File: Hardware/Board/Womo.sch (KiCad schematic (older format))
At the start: 0 parts

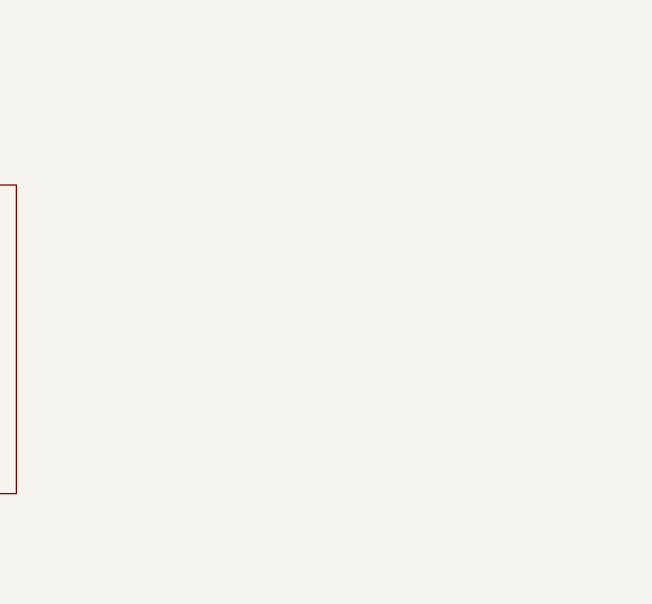
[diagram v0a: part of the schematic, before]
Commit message: FTDI EVE Touch hinzugefügt
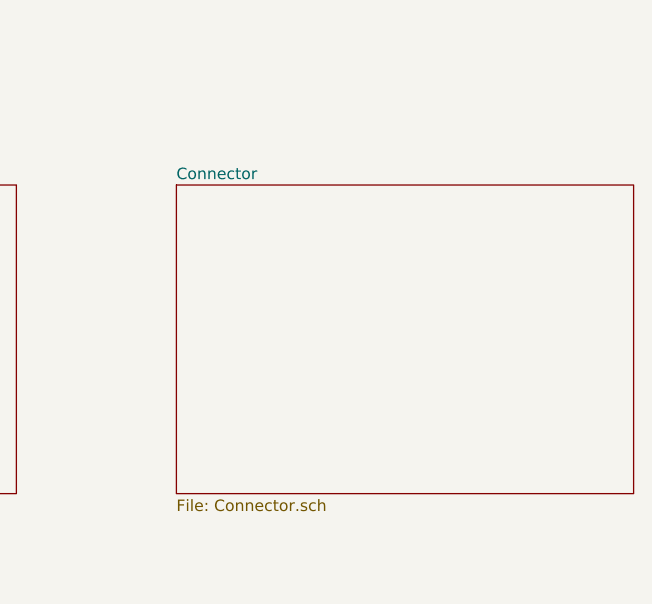
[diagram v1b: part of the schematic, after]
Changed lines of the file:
@@
 $Descr A4 11693 8268
 encoding utf-8
-Sheet 1 6
+Sheet 1 7
 Title ""
 Date ""
@@
 F1 "Sensor.sch" 50
 $EndSheet
+$Sheet
+S 6850 3450 2000 1350
+U 5CC9A992
+F0 "Connector" 50
+F1 "Connector.sch" 50
+$EndSheet
 $EndSCHEMATC

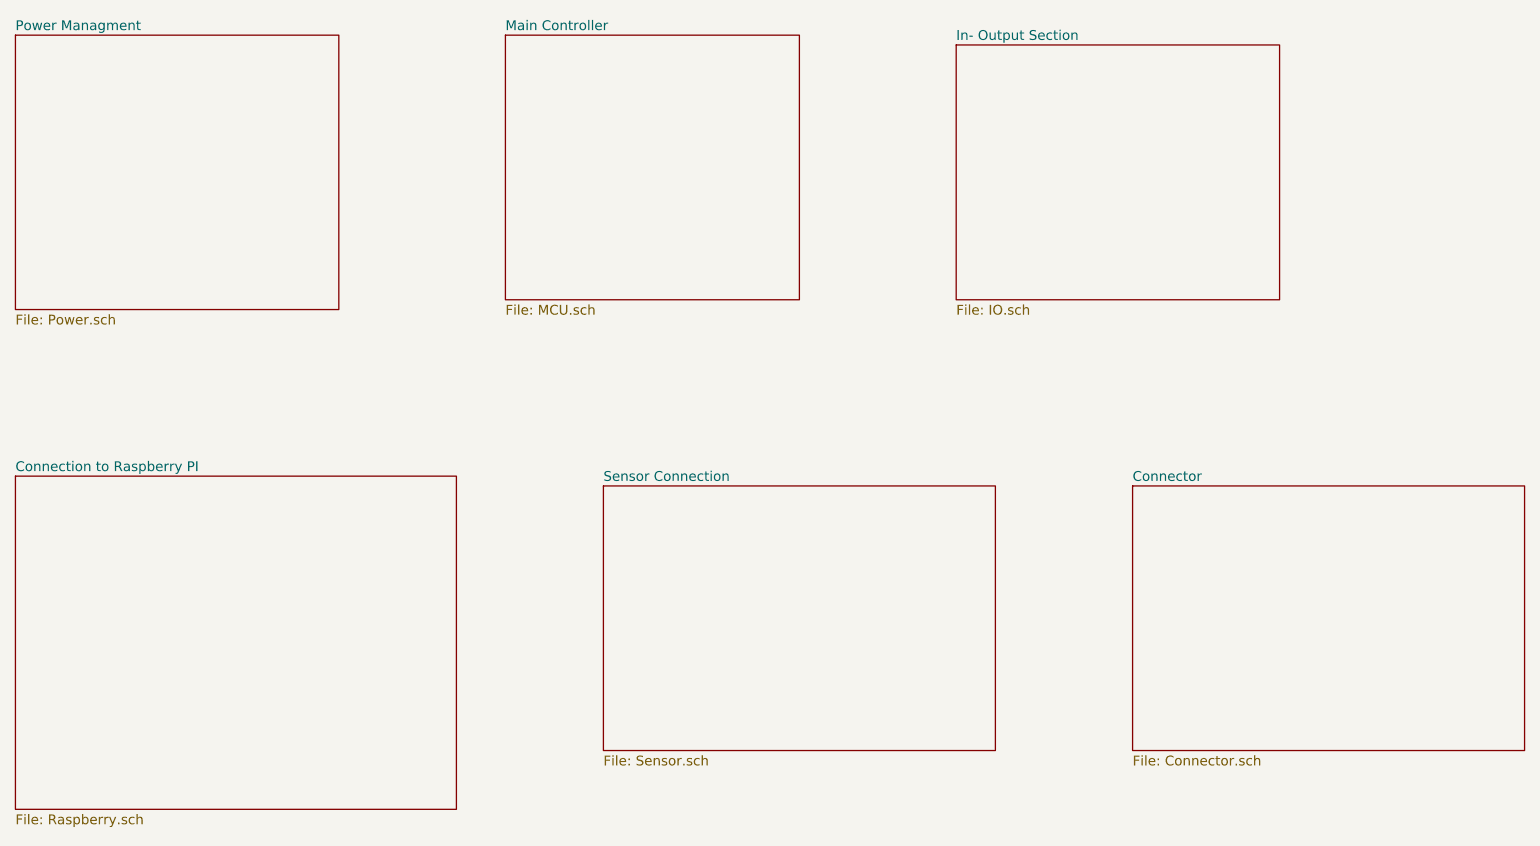
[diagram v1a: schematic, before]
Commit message: Netzliste und Board erstellt, hier sind noch Fehler im Bereich Footprints, BLE Modul nRF8001 hinzugefügt, erste Anschlussklemmen zugefügt
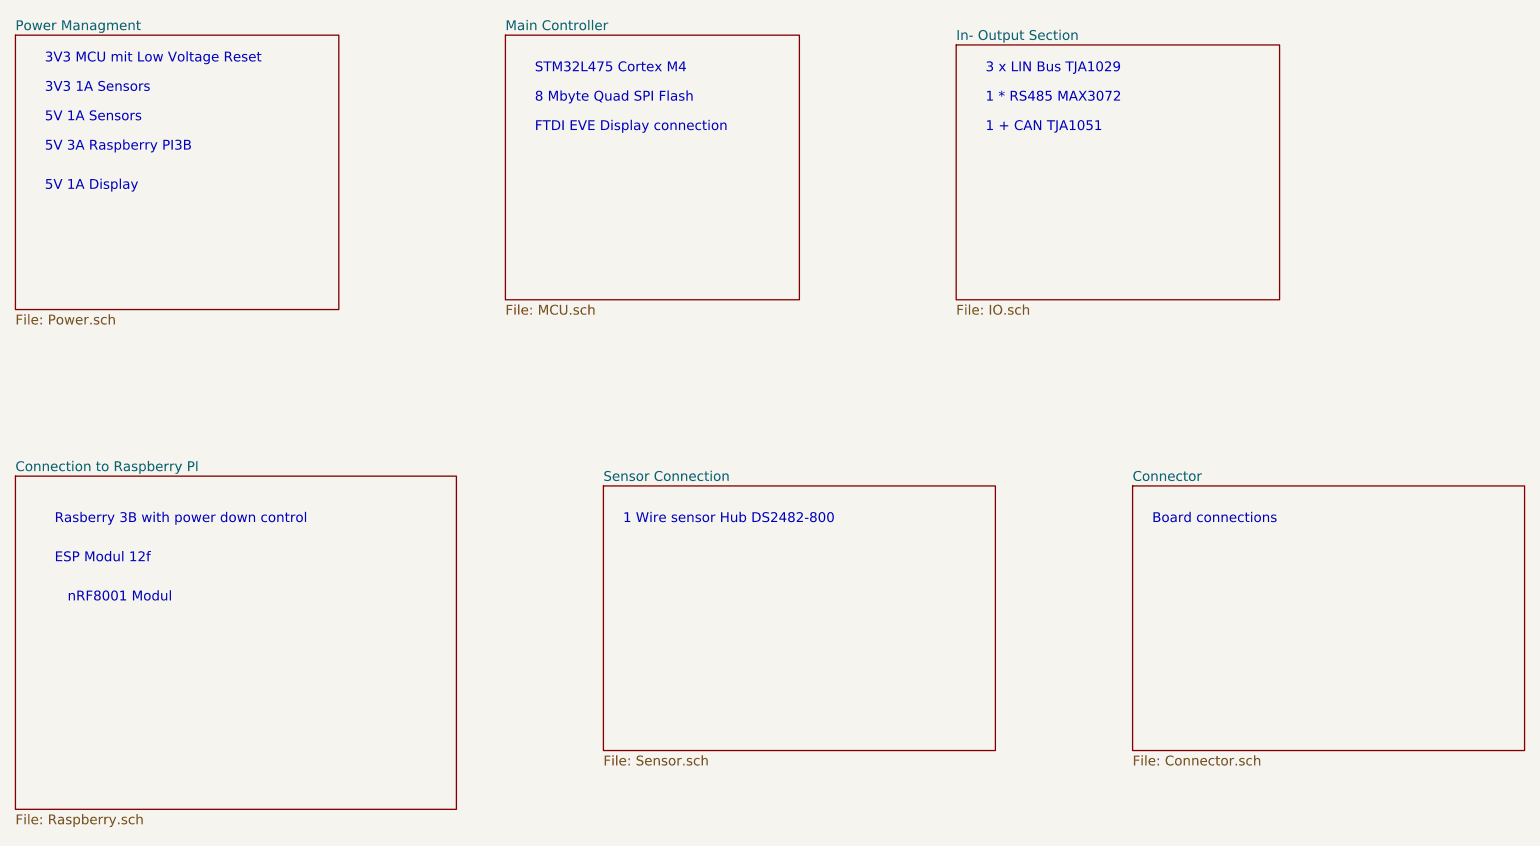
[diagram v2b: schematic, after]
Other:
- note added: "1 * RS485 MAX3072\n"
- note added: "1 + CAN TJA1051\n"
- note added: "1 Wire sensor Hub DS2482-800"
- note added: "3 x LIN Bus TJA1029\n"
- note added: "3V3 1A Sensors"
- note added: "3V3 MCU mit Low Voltage Reset"
- note added: "5V 1A Display"
- note added: "5V 1A Sensors"
- note added: "5V 3A Raspberry PI3B"
- note added: "8 Mbyte Quad SPI Flash\n"
- note added: "Board connections"
- note added: "ESP Modul 12f"
- note added: "FTDI EVE Display connection\n"
- note added: "Rasberry 3B with power down control"
- note added: "STM32L475 Cortex M4\n"
- note added: "nRF8001 Modul\n"
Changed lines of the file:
@@
 F1 "Connector.sch" 50
 $EndSheet
+Text Notes 1300 1300 0    50   ~ 0
+3V3 MCU mit Low Voltage Reset
+Text Notes 1300 1450 0    50   ~ 0
+3V3 1A Sensors
+Text Notes 1300 1600 0    50   ~ 0
+5V 1A Sensors
+Text Notes 1300 1750 0    50   ~ 0
+5V 3A Raspberry PI3B
+Text Notes 1300 1950 0    50   ~ 0
+5V 1A Display
+Text Notes 3800 1350 0    50   ~ 0
+STM32L475 Cortex M4\n
+Text Notes 3800 1500 0    50   ~ 0
+8 Mbyte Quad SPI Flash\n
+Text Notes 3800 1650 0    50   ~ 0
+FTDI EVE Display connection\n
+Text Notes 6100 1350 0    50   ~ 0
+3 x LIN Bus TJA1029\n
+Text Notes 6100 1500 0    50   ~ 0
+1 * RS485 MAX3072\n
+Text Notes 6100 1650 0    50   ~ 0
+1 + CAN TJA1051\n
+Text Notes 1350 3650 0    50   ~ 0
+Rasberry 3B with power down control
+Text Notes 1350 3850 0    50   ~ 0
+ESP Modul 12f
+Text Notes 4250 3650 0    50   ~ 0
+1 Wire sensor Hub DS2482-800
+Text Notes 6950 3650 0    50   ~ 0
+Board connections
+Text Notes 1950 4050 2    50   ~ 0
+nRF8001 Modul\n
 $EndSCHEMATC

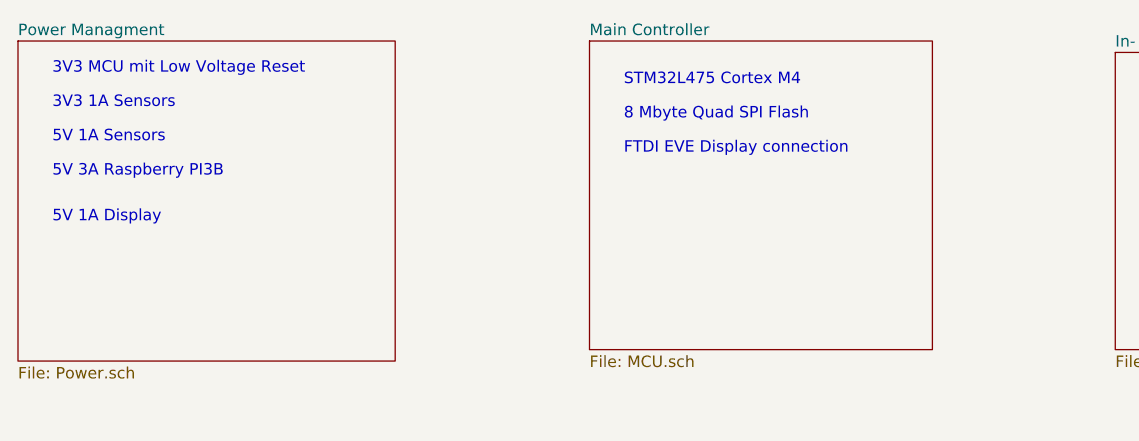
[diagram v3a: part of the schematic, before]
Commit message: Octo SPI Flash und RAM zugefügt, weitere Bezeichnungen auf Stand gebracht
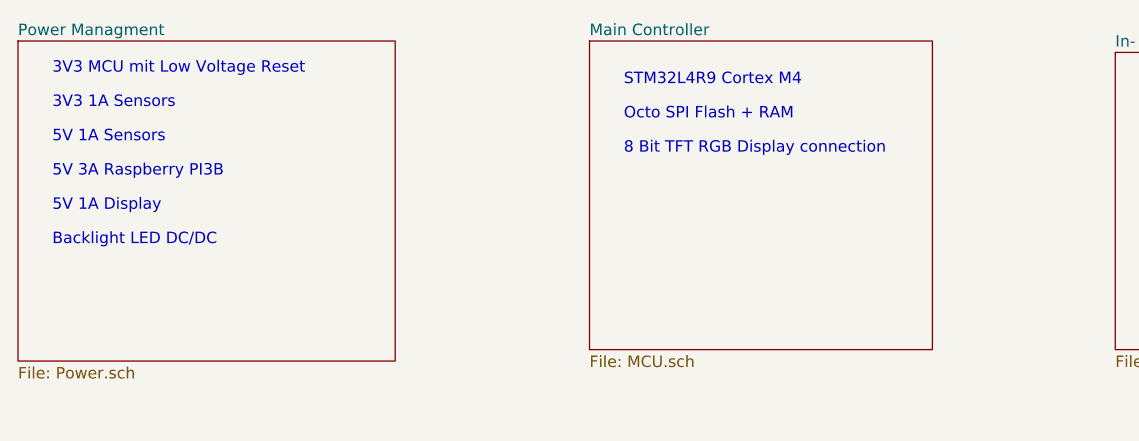
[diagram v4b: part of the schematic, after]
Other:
- note added: "8 Bit TFT RGB Display connection\n"
- note added: "Backlight LED DC/DC"
- note added: "Octo SPI Flash + RAM\n"
- note added: "STM32L4R9 Cortex M4\n"
- note removed: "8 Mbyte Quad SPI Flash\n"
- note removed: "FTDI EVE Display connection\n"
- note removed: "STM32L475 Cortex M4\n"
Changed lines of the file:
@@
 Text Notes 1300 1750 0    50   ~ 0
 5V 3A Raspberry PI3B
-Text Notes 1300 1950 0    50   ~ 0
+Text Notes 1300 1900 0    50   ~ 0
 5V 1A Display
 Text Notes 3800 1350 0    50   ~ 0
-STM32L475 Cortex M4\n
+STM32L4R9 Cortex M4\n
 Text Notes 3800 1500 0    50   ~ 0
-8 Mbyte Quad SPI Flash\n
+Octo SPI Flash + RAM\n
 Text Notes 3800 1650 0    50   ~ 0
-FTDI EVE Display connection\n
+8 Bit TFT RGB Display connection\n
 Text Notes 6100 1350 0    50   ~ 0
 3 x LIN Bus TJA1029\n
@@
 F1 "MCU.sch" 50
 $EndSheet
+Text Notes 1300 2050 0    50   ~ 0
+Backlight LED DC/DC
 $EndSCHEMATC

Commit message: Eine Menge Arbeit auf der GPN, fast fertig im Schaltplan.
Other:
- note added: "I2C Power Managment"
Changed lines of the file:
@@
 EESchema Schematic File Version 4
 LIBS:Womo-cache
-EELAYER 26 0
+EELAYER 29 0
 EELAYER END
 $Descr A4 11693 8268
@@
 Text Notes 1300 2050 0    50   ~ 0
 Backlight LED DC/DC
+Text Notes 6100 1800 0    50   ~ 0
+I2C Power Managment
 $EndSCHEMATC

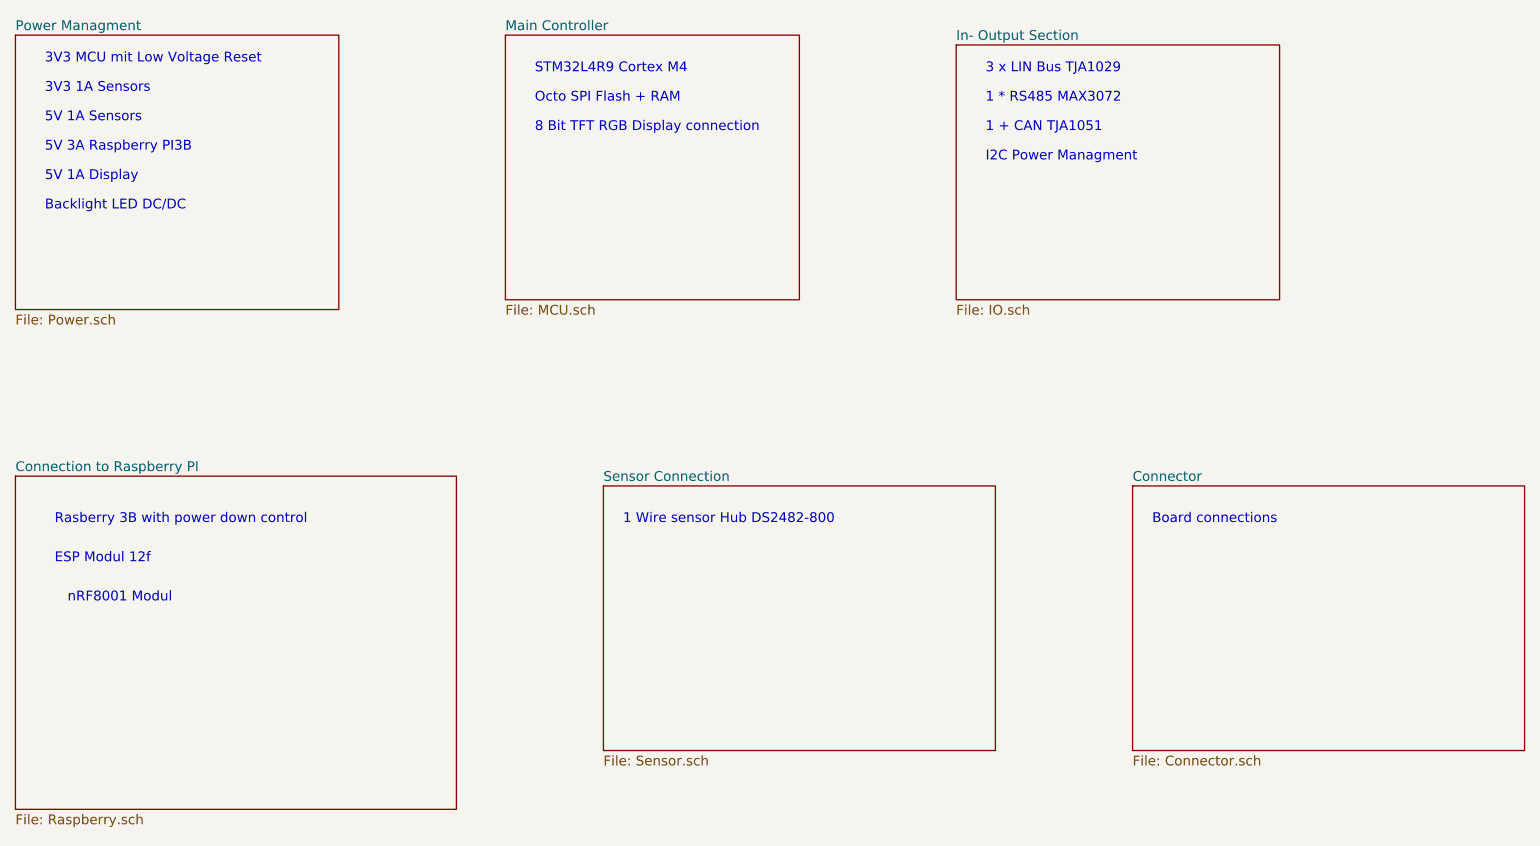
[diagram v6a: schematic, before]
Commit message: MCU Section fertig, Analog Inputs angelegt, Schaltplan neu organisiert, alte Datenblätter entfernt.
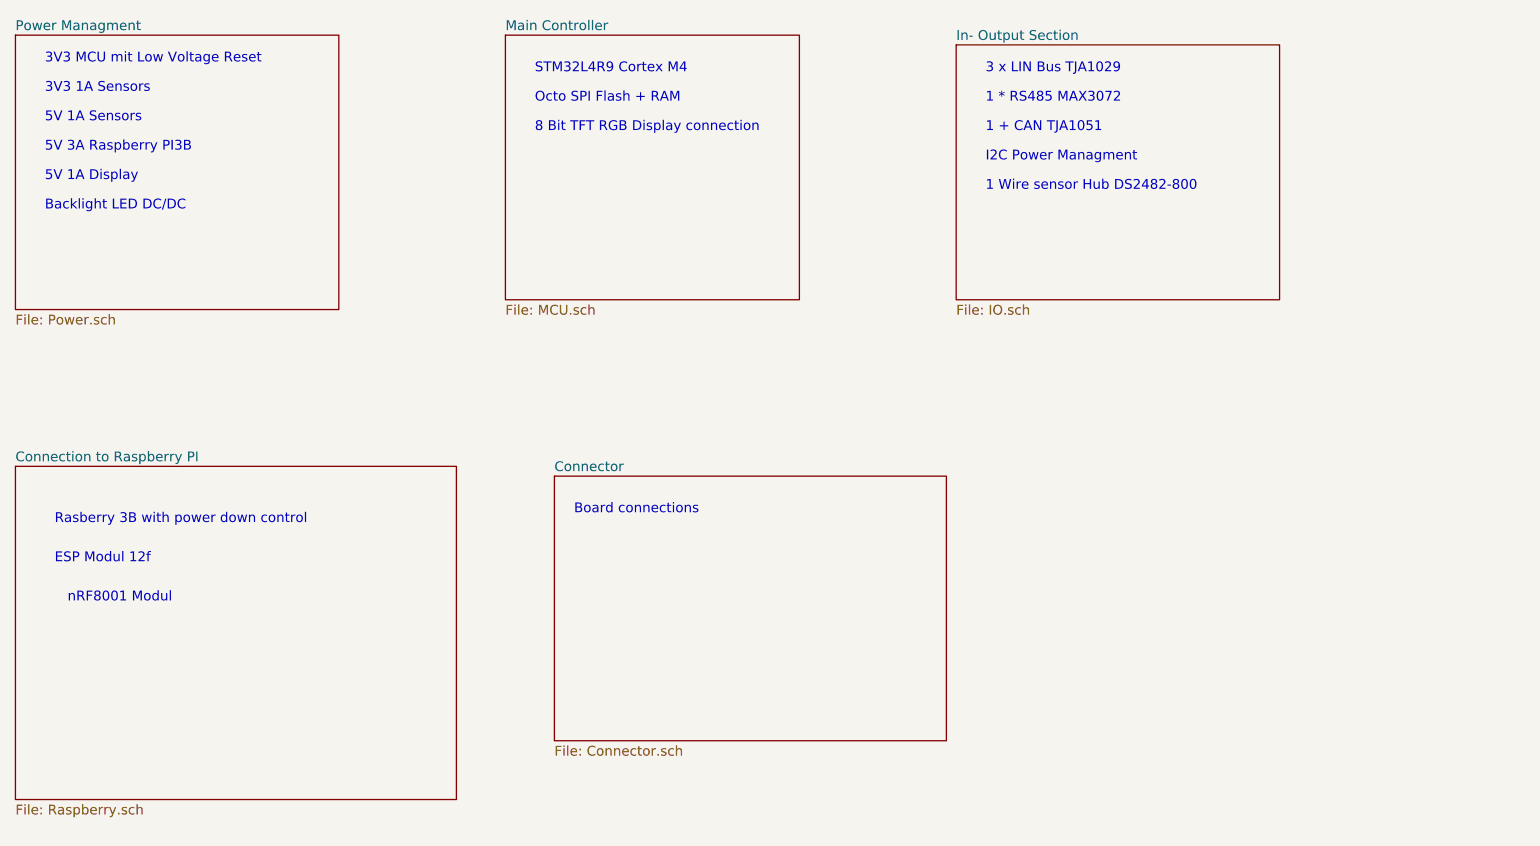
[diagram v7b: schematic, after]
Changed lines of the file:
@@
 $Descr A4 11693 8268
 encoding utf-8
-Sheet 1 7
+Sheet 1 6
 Title ""
 Date ""
@@
 $EndSheet
 $Sheet
-S 1150 3400 2250 1700
+S 1150 3350 2250 1700
 U 5C8BC88B
 F0 "Connection to Raspberry PI" 50
@@
 $EndSheet
 $Sheet
-S 4150 3450 2000 1350
-U 5C9E4308
-F0 "Sensor Connection" 50
-F1 "Sensor.sch" 50
-$EndSheet
-$Sheet
-S 6850 3450 2000 1350
+S 3900 3400 2000 1350
 U 5CC9A992
 F0 "Connector" 50
@@
 Text Notes 1350 3850 0    50   ~ 0
 ESP Modul 12f
-Text Notes 4250 3650 0    50   ~ 0
+Text Notes 6100 1950 0    50   ~ 0
 1 Wire sensor Hub DS2482-800
-Text Notes 6950 3650 0    50   ~ 0
+Text Notes 4000 3600 0    50   ~ 0
 Board connections
 Text Notes 1950 4050 2    50   ~ 0

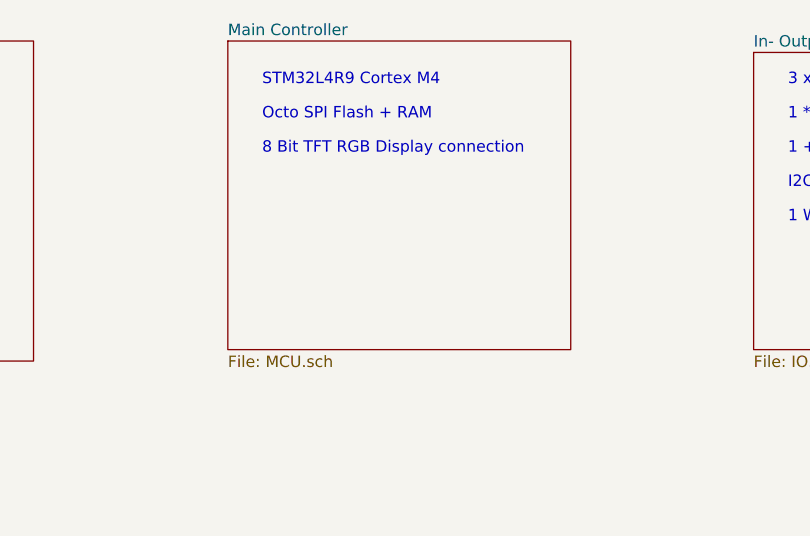
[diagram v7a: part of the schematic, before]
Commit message: Trennung MCU und Rest, Footprints fast alles zugewiesen, GSM Modul integriert, viel Kleinkram
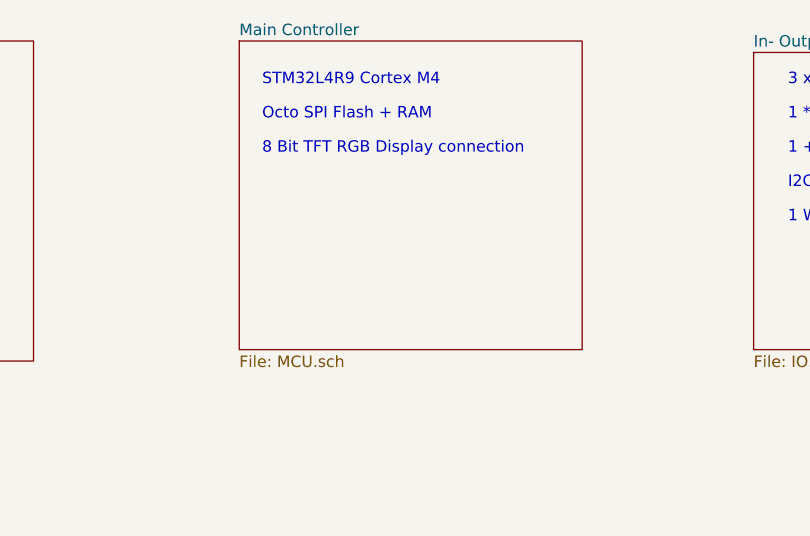
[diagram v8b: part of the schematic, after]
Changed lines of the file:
@@
 nRF8001 Modul\n
 $Sheet
-S 3650 1150 1500 1350
+S 3700 1150 1500 1350
 U 5C8BBC94
 F0 "Main Controller" 50
